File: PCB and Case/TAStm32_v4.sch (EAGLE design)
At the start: 40 parts, among them IC1 74AVCH4T245PW,118, IC2 74AVCH4T245PW,118, IC3 74AVCH4T245PW,118, J1 ZX62D-B-5PA8, J10 RJSSE538002_RJSSE538002, J11 RJSSE538002_RJSSE538002, J12 SOICBITE, J13 CONSOLE_RESET, J2 UE27-AC54-100, J3 OLED128X64, J4 CONSOLE_RESET, J5 95278-802A12LF, J6 SAMTEC-TSM-106-01-X-SV_SAMTEC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, J7 SAMTEC-TSM-106-01-X-SV_SAMTEC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, J8 SAMTEC-TSM-106-01-X-SV_SAMTEC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, J9 SAMTEC-TSM-106-01-X-SV_SAMTEC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, U1 STM32F446RET6, U2 3.3V REG, Y1 8MHz

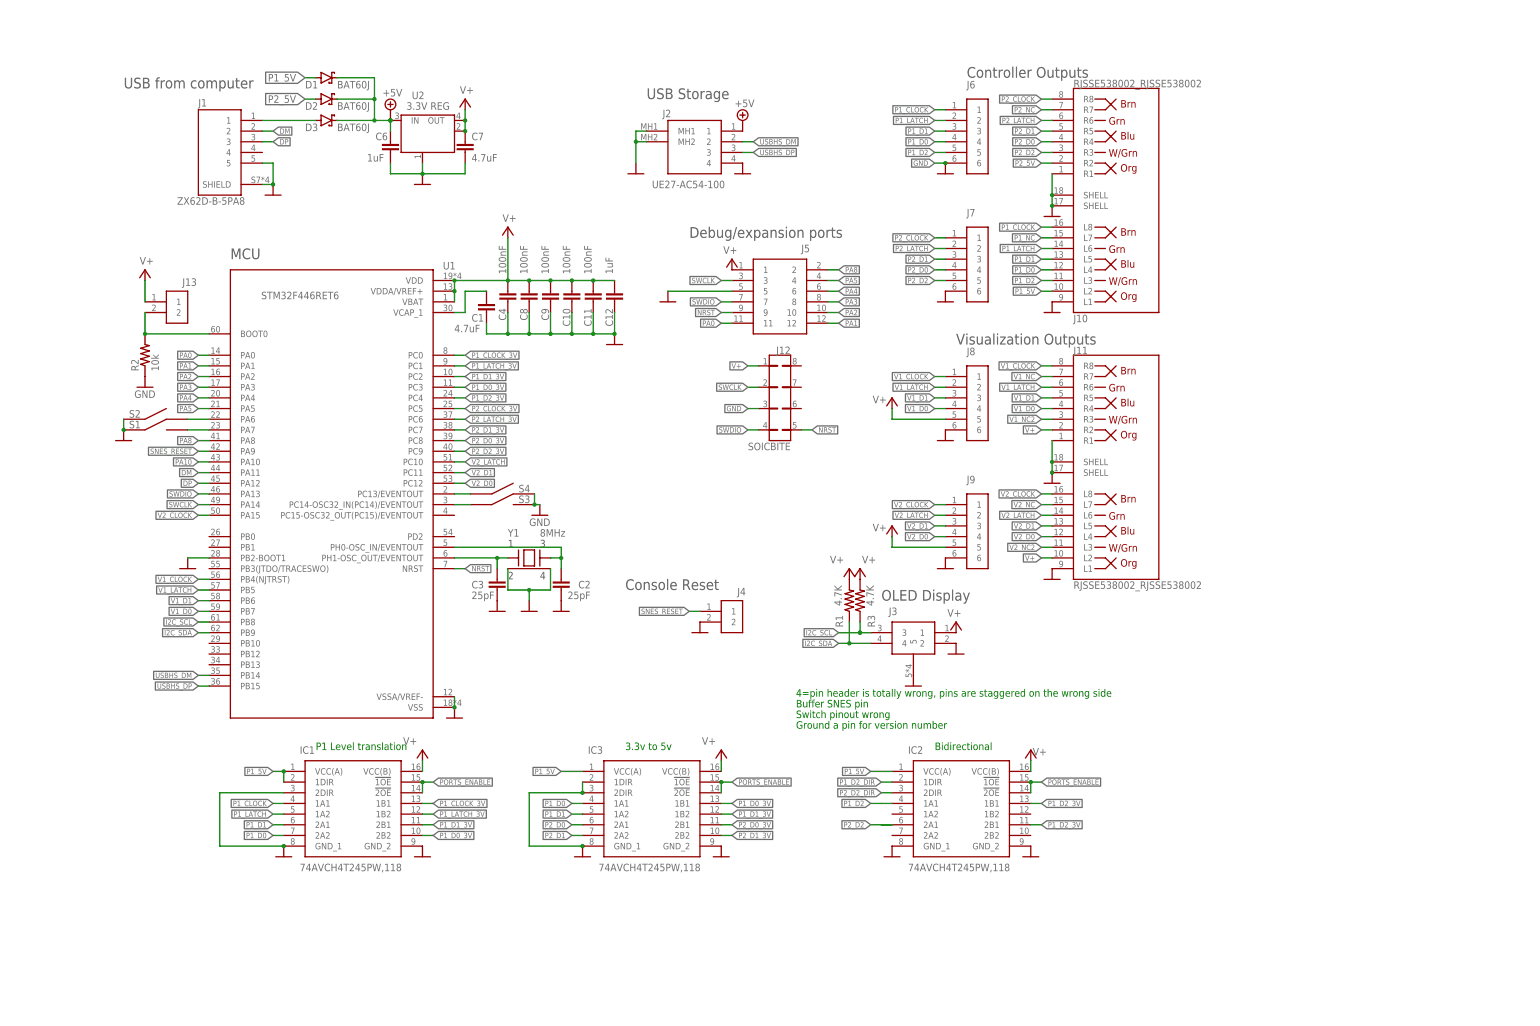
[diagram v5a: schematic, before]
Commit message: different level translators
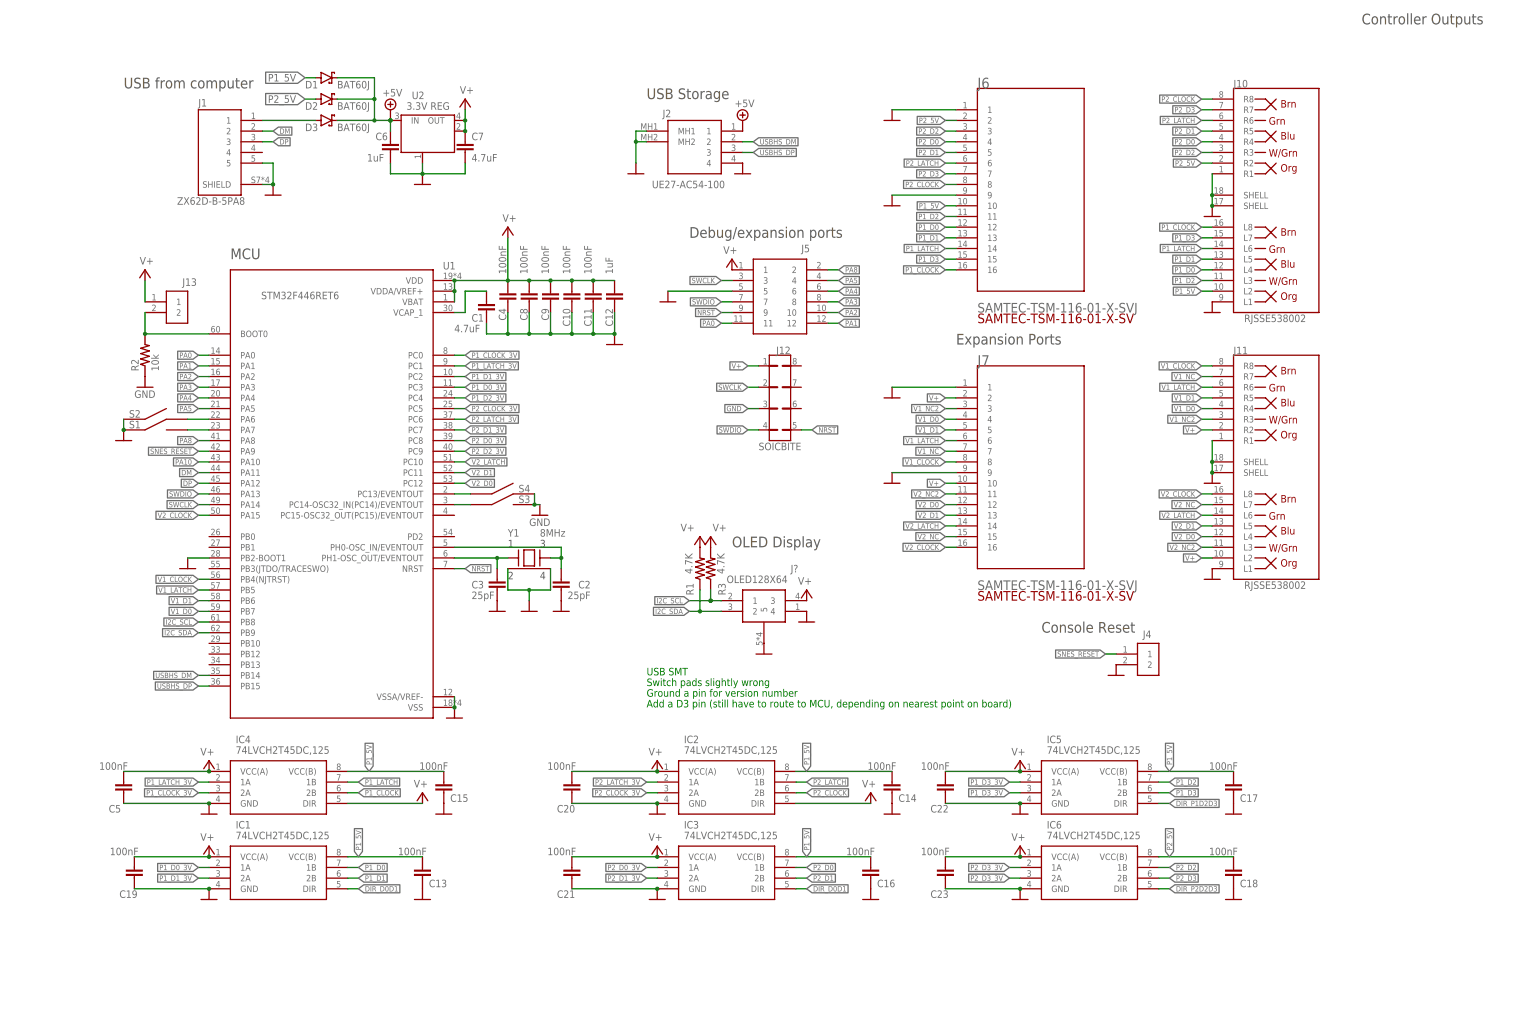
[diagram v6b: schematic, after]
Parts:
- removed J3: OLED128X64, TAStm32_v4:OLED128X64
- removed J8, J9: SAMTEC-TSM-106-01-X-SV_SAMTEC-TSM-106-01-X-SV, TAStm32_v4:SAMTEC-TSM-106-01-X-SV_SAMTEC-TSM-106-01-X-SV
- added C13, C14, C15, C16, C17, C18, C19, C20, C21, C22, C23, C5: 100nF, rcl:C-EUC0603K
- added IC4, IC5, IC6: 74LVCH2T45DC,125, SamacSys_Parts:74LVCH2T45DC,125
- added J?: OLED128X64, TAStm32_v4:OLED128X64
- C1, C10, C11, C12, C2, C3, C4, C6, C7, C8, C9: device rcl:C-EUC0805K -> rcl:C-EUC0603K
- IC1, IC2, IC3: value 74AVCH4T245PW,118 -> 74LVCH2T45DC,125; device SamacSys_Parts:74AVCH4T245PW,118 -> SamacSys_Parts:74LVCH2T45DC,125
- J10, J11: value RJSSE538002_RJSSE538002 -> RJSSE538002
- J6, J7: value SAMTEC-TSM-106-01-X-SV_SAMTEC-TSM-106-01-X-SV -> SAMTEC-TSM-116-01-X-SVJ; device TAStm32_v4:SAMTEC-TSM-106-01-X-SV_SAMTEC-TSM-106-01-X-SV -> SAMTEC-TSM-116-01-X-SV:SAMTEC-TSM-116-01-X-SVJ
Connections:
- removed net N$11: IC2.2A1
- removed net P1_D2_DIR: IC2.1DIR
- removed net P1_NC: J10.L7
- removed net P2_D2_DIR: IC2.2DIR
- removed net P2_NC: J10.R7
- removed net PORTS_ENABLE: IC1.!1OE, IC1.!2OE, IC2.!1OE, IC2.!2OE, IC3.!1OE, IC3.!2OE
- new net DIR_D0D1: IC1.DIR, IC3.DIR
- new net DIR_P1D2D3: IC5.DIR
- new net DIR_P2D2D3: IC6.DIR
- new net N$8: IC5.2A
- new net P1_D3: IC5.2B, J10.L7, J6.15
- new net P1_D3_3V: IC5.1A
- new net P2_D3: IC6.2B, J10.R7, J6.7
- new net P2_D3_3V: IC6.1A
- net GND: now also C13.1, C14.1, C15.1, C16.1, C17.1, C18.1, C19.1, C20.1, C21.1, C22.1, C23.1, C5.1, IC1.GND, IC2.GND, IC3.GND, IC4.GND, IC5.GND, IC6.GND, J6.1, J6.9, J7.1, J7.9, J?.4, J?.5; no longer IC1.2DIR, IC1.GND_1, IC1.GND_2, IC2.GND_1, IC2.GND_2, IC3.1DIR, IC3.2DIR, IC3.GND_1, IC3.GND_2, J3.2, J3.5, J6.6, J7.6, J8.6, J9.6
- net I2C_SCL: now also J?.1; no longer J3.3
- net I2C_SDA: now also J?.2; no longer J3.4
- net N$9: now also IC6.2A; no longer IC2.1A1
- net P1_5V: now also C13.2, C14.2, C15.2, C16.2, C17.2, IC1.VCC(B), IC2.VCC(B), IC3.VCC(B), IC4.VCC(B), IC5.VCC(B), J6.10; no longer IC1.1DIR, IC1.VCC(A), IC2.VCC(A), IC3.VCC(A)
- net P1_CLOCK: now also IC4.2B, J6.16; no longer IC1.1A1, J6.1
- net P1_CLOCK_3V: now also IC4.2A; no longer IC1.1B1
- net P1_D0: now also IC1.1B, J6.12; no longer IC1.2A2, IC3.1A1, J6.4
- net P1_D0_3V: now also IC1.1A; no longer IC1.2B2, IC3.1B1
- net P1_D1: now also IC1.2B, J6.13; no longer IC1.2A1, IC3.1A2, J6.3
- net P1_D1_3V: now also IC1.2A; no longer IC1.2B1, IC3.1B2
- net P1_D2: now also IC5.1B, J6.11; no longer J6.5
- net P1_D2_3V: no longer IC2.1B1, IC2.2B1
- net P1_LATCH: now also IC4.1B, J6.14; no longer IC1.1A2, J6.2
- net P1_LATCH_3V: now also IC4.1A; no longer IC1.1B2
- net P2_5V: now also C18.2, IC6.VCC(B), J6.2
- net P2_CLOCK: now also IC2.2B, J6.8; no longer J7.1
- net P2_CLOCK_3V: now also IC2.2A
- net P2_D0: now also IC3.1B, J6.4; no longer IC3.2A1, J7.4
- net P2_D0_3V: now also IC3.1A; no longer IC3.2B1
- net P2_D1: now also IC3.2B, J6.5; no longer IC3.2A2, J7.3
- net P2_D1_3V: now also IC3.2A; no longer IC3.2B2
- net P2_D2: now also IC6.1B, J6.3; no longer J7.5
- net P2_LATCH: now also IC2.1B, J6.6; no longer J7.2
- net P2_LATCH_3V: now also IC2.1A
- net V+: now also C19.2, C20.2, C21.2, C22.2, C23.2, C5.2, IC1.VCC(A), IC2.DIR, IC2.VCC(A), IC3.VCC(A), IC4.DIR, IC4.VCC(A), IC5.VCC(A), IC6.VCC(A), J7.10, J7.2, J?.3; no longer IC1.VCC(B), IC2.VCC(B), IC3.VCC(B), J3.1, J8.5, J9.5
- net V1_CLOCK: now also J7.8; no longer J8.1
- net V1_D0: now also J7.4; no longer J8.4
- net V1_D1: now also J7.5; no longer J8.3
- net V1_LATCH: now also J7.6; no longer J8.2
- net V1_NC: now also J7.7
- net V1_NC2: now also J7.3
- net V2_CLOCK: now also J7.16; no longer J9.1
- net V2_D0: now also J7.12; no longer J9.4
- net V2_D1: now also J7.13; no longer J9.3
- net V2_LATCH: now also J7.14; no longer J9.2
- net V2_NC: now also J7.15
- net V2_NC2: now also J7.11
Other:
- note added: "Add a D3 pin (still have to route to MCU, depending on nearest point on board)"
- note added: "Expansion Ports"
- note added: "Switch pads slightly wrong"
- note added: "USB SMT"
- note removed: "3.3v to 5v"
- note removed: "4=pin header is totally wrong, pins are staggered on the wrong side"
- note removed: "Bidirectional"
- note removed: "Buffer SNES pin"
- note removed: "P1 Level translation"
- note removed: "Switch pinout wrong"
- note removed: "Visualization Outputs"
- moved on the sheet: J10, J11, J4, R1, R3

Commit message: notes
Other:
- note added: "Maybe make debug/expansion header SIL to make it fit better"
- note removed: "USB SMT"
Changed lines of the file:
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@@
 <text x="-17.78" y="-60.96" size="1.778" layer="91">Ground a pin for version number</text>
 <text x="-17.78" y="-63.5" size="1.778" layer="91">Add a D3 pin (still have to route to MCU, depending on nearest point on board)</text>
-<text x="-17.78" y="-55.88" size="1.778" layer="91">USB SMT</text>
+<text x="-17.78" y="-55.88" size="1.778" layer="91">Maybe make debug/expansion header SIL to make it fit better</text>
 </plain>
 <instances>

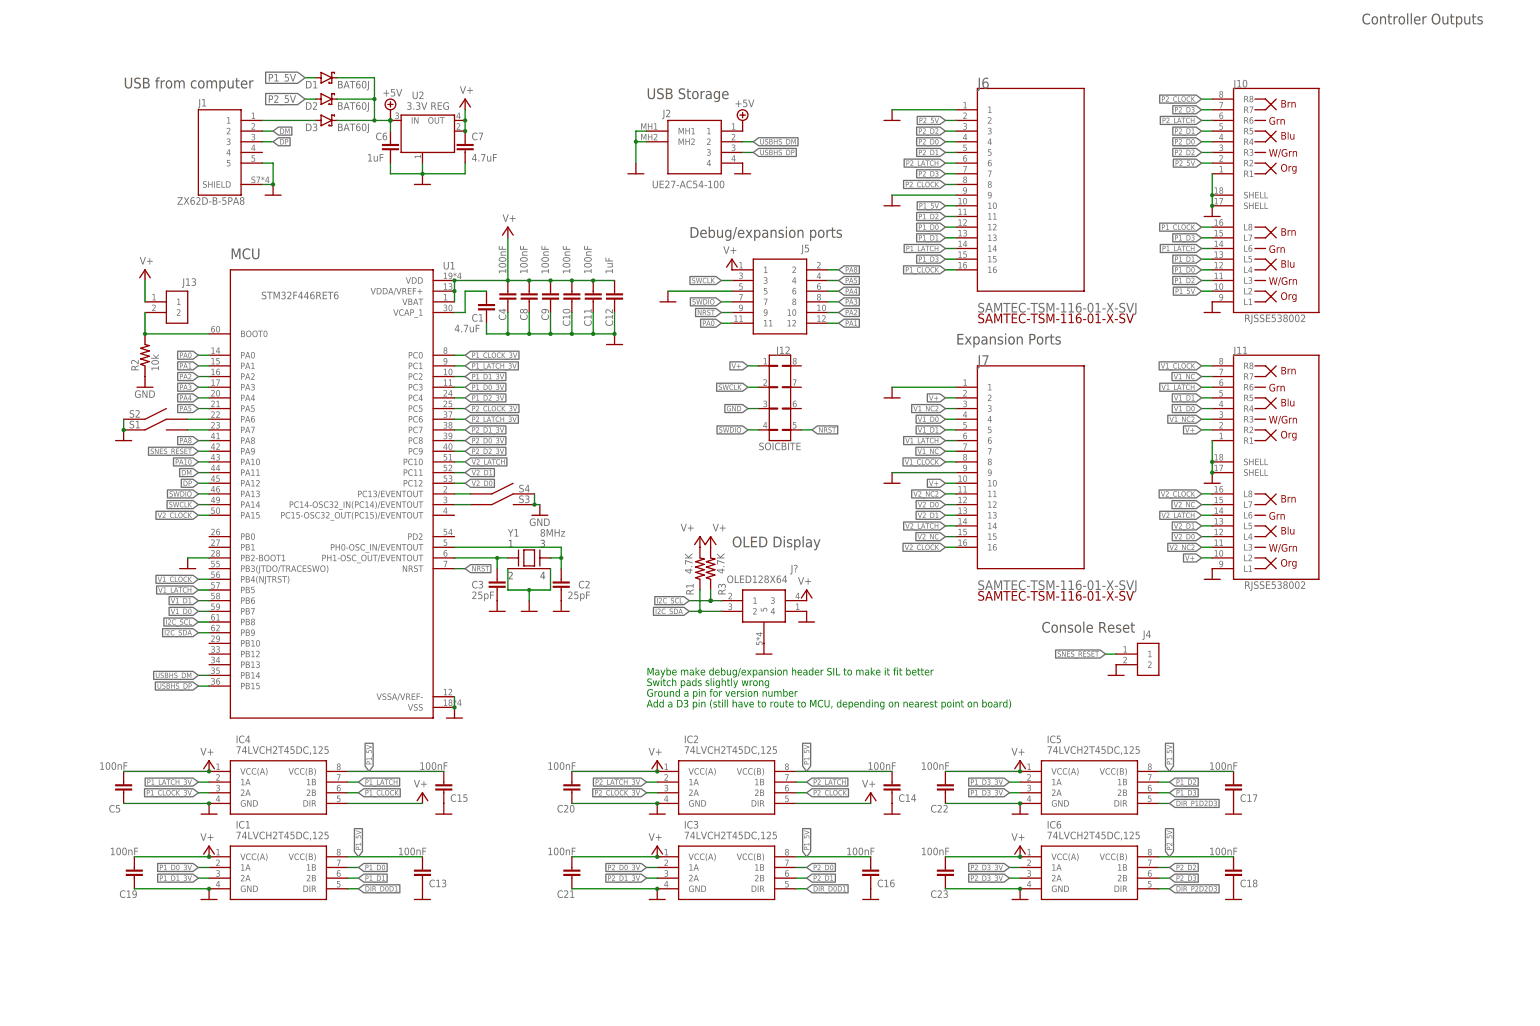
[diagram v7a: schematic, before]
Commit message: another different level converter, routing
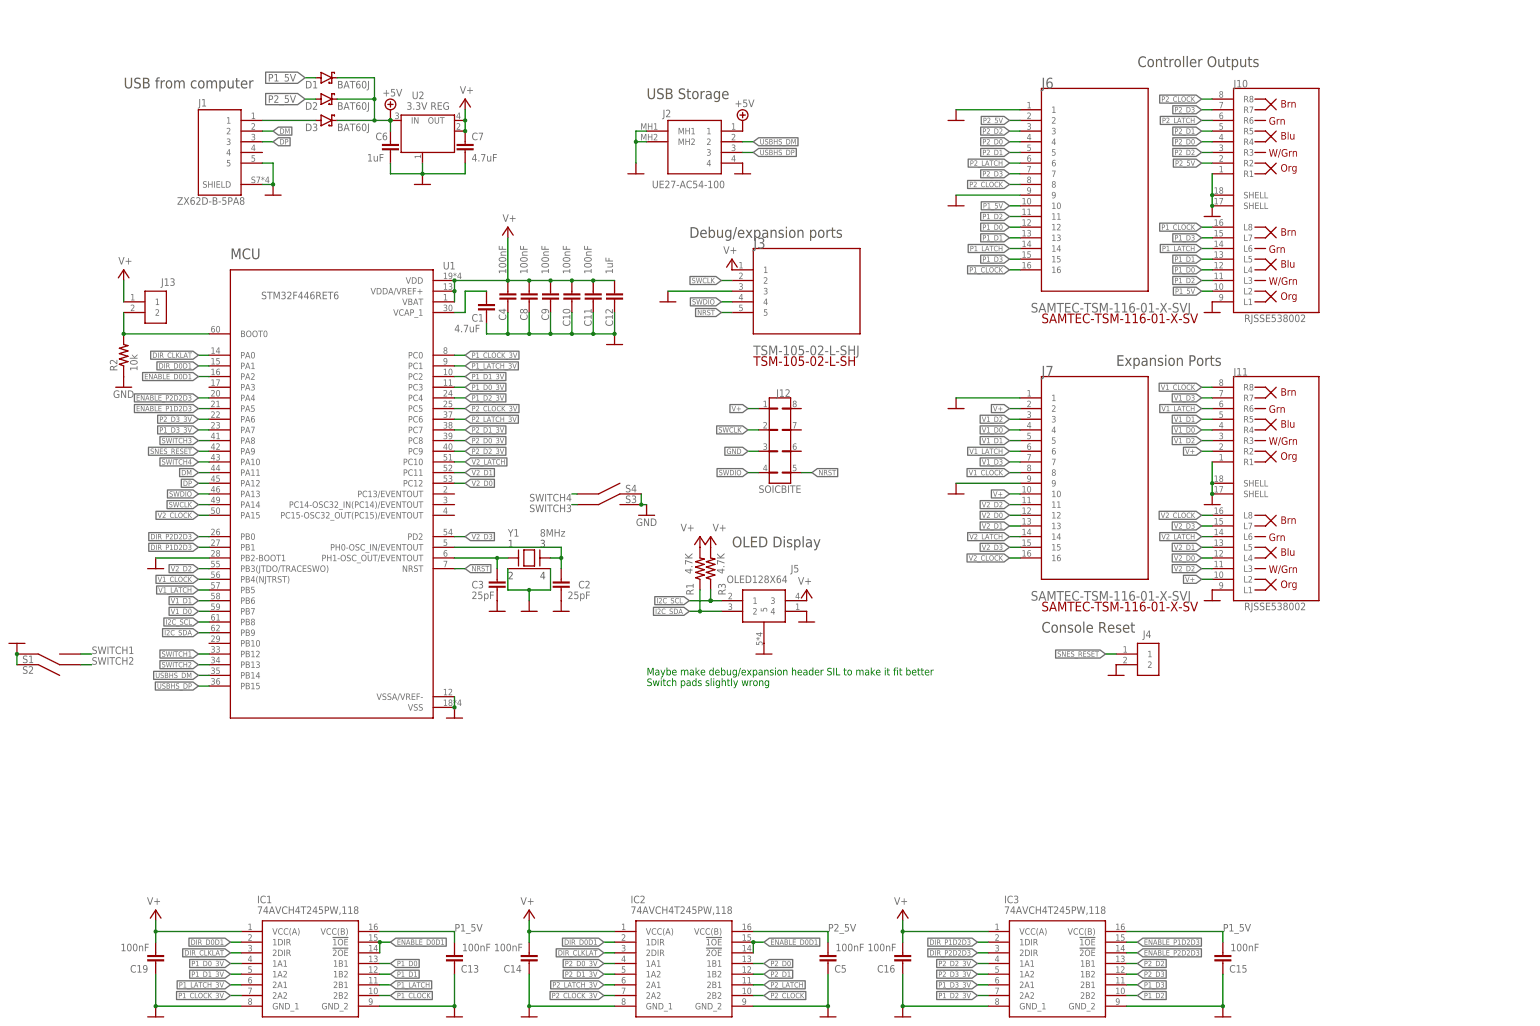
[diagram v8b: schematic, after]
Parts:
- removed C17, C18, C20, C21, C22, C23: 100nF, rcl:C-EUC0603K
- removed IC4, IC5, IC6: 74LVCH2T45DC,125, SamacSys_Parts:74LVCH2T45DC,125
- removed J?: OLED128X64, TAStm32_v4:OLED128X64
- added J3: TSM-105-02-L-SHJ, TSM-105-02-L-SH:TSM-105-02-L-SHJ
- IC1, IC2, IC3: value 74LVCH2T45DC,125 -> 74AVCH4T245PW,118; device SamacSys_Parts:74LVCH2T45DC,125 -> SamacSys_Parts:74AVCH4T245PW,118
- J5: value 95278-802A12LF -> OLED128X64; device SamacSys_Parts:95278-802A12LF -> TAStm32_v4:OLED128X64
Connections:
- net V1_NC renamed V1_D3
- net V1_NC2 renamed V1_D2
- removed net N$2: S4.P$1, U1.PC13/EVENTOUT
- removed net N$3: S3.P$1, U1.PC14-OSC32_IN(PC14)/EVENTOUT
- removed net N$4: S2.P$2, U1.PA6
- removed net N$6: S1.P$2, U1.PA7
- removed net N$8: IC5.2A
- removed net N$9: IC6.2A
- removed net PA0: J5.11, U1.PA0
- removed net PA1: J5.12, U1.PA1
- removed net PA10: U1.PA10
- removed net PA2: J5.10, U1.PA2
- removed net PA3: J5.8, U1.PA3
- removed net PA4: J5.6, U1.PA4
- removed net PA5: J5.4, U1.PA5
- removed net PA8: J5.2, U1.PA8
- removed net V2_NC: J11.L7, J7.15
- removed net V2_NC2: J11.L3, J7.11
- new net DIR_CLKLAT: IC1.2DIR, IC2.2DIR, U1.PA0
- new net ENABLE_D0D1: IC1.!1OE, IC1.!2OE, IC2.!1OE, IC2.!2OE, U1.PA2
- new net ENABLE_P1D2D3: IC3.!1OE, U1.PA5
- new net ENABLE_P2D2D3: IC3.!2OE, U1.PA4
- new net SWITCH1: S1.P$2, U1.PB12
- new net SWITCH2: S2.P$2, U1.PB13
- new net SWITCH3: S3.P$1, U1.PA8
- new net SWITCH4: S4.P$1, U1.PA10
- new net V2_D2: J11.L3, J7.11, U1.PB3(JTDO/TRACESWO)
- new net V2_D3: J11.L7, J7.15, U1.PD2
- net DIR_D0D1: now also IC1.1DIR, IC2.1DIR, U1.PA1; no longer IC1.DIR, IC3.DIR
- net DIR_P1D2D3: now also IC3.1DIR, U1.PB1; no longer IC5.DIR
- net DIR_P2D2D3: now also IC3.2DIR, U1.PB0; no longer IC6.DIR
- net GND: now also IC1.GND_1, IC1.GND_2, IC2.GND_1, IC2.GND_2, IC3.GND_1, IC3.GND_2, J3.3, J5.4; no longer C17.1, C18.1, C20.1, C21.1, C22.1, C23.1, IC1.GND, IC2.GND, IC3.GND, IC4.GND, IC5.GND, IC6.GND, J?.4, J?.5
- net I2C_SCL: now also J5.1; no longer J?.1
- net I2C_SDA: now also J5.2; no longer J?.2
- net NRST: now also J3.5; no longer J5.9
- net P1_5V: no longer C14.2, C16.2, C17.2, IC2.VCC(B), IC4.VCC(B), IC5.VCC(B)
- net P1_CLOCK: now also IC1.2B2; no longer IC4.2B
- net P1_CLOCK_3V: now also IC1.2A2; no longer IC4.2A
- net P1_D0: now also IC1.1B1; no longer IC1.1B
- net P1_D0_3V: now also IC1.1A1; no longer IC1.1A
- net P1_D1: now also IC1.1B2; no longer IC1.2B
- net P1_D1_3V: now also IC1.1A2; no longer IC1.2A
- net P1_D2: now also IC3.2B2; no longer IC5.1B
- net P1_D2_3V: now also IC3.2A2
- net P1_D3: now also IC3.2B1; no longer IC5.2B
- net P1_D3_3V: now also IC3.2A1, U1.PA7; no longer IC5.1A
- net P1_LATCH: now also IC1.2B1; no longer IC4.1B
- net P1_LATCH_3V: now also IC1.2A1; no longer IC4.1A
- net P2_5V: now also C5.2, IC2.VCC(B); no longer C18.2, IC6.VCC(B)
- net P2_CLOCK: now also IC2.2B2; no longer IC2.2B
- net P2_CLOCK_3V: now also IC2.2A2; no longer IC2.2A
- net P2_D0: now also IC2.1B1; no longer IC3.1B
- net P2_D0_3V: now also IC2.1A1; no longer IC3.1A
- net P2_D1: now also IC2.1B2; no longer IC3.2B
- net P2_D1_3V: now also IC2.1A2; no longer IC3.2A
- net P2_D2: now also IC3.1B1; no longer IC6.1B
- net P2_D2_3V: now also IC3.1A1
- net P2_D3: now also IC3.1B2; no longer IC6.2B
- net P2_D3_3V: now also IC3.1A2, U1.PA6; no longer IC6.1A
- net P2_LATCH: now also IC2.2B1; no longer IC2.1B
- net P2_LATCH_3V: now also IC2.2A1; no longer IC2.1A
- net SWCLK: now also J3.2; no longer J5.3
- net SWDIO: now also J3.4; no longer J5.7
- net V+: now also C14.2, C16.2, J3.1, J5.3; no longer C20.2, C21.2, C22.2, C23.2, C5.2, IC2.DIR, IC4.DIR, IC4.VCC(A), IC5.VCC(A), IC6.VCC(A), J5.1, J?.3
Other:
- note removed: "Add a D3 pin (still have to route to MCU, depending on nearest point on board)"
- note removed: "Ground a pin for version number"
- moved on the sheet: C13, C14, C15, C16, C19, C5, J11, J12, J13, J6, J7, R2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
